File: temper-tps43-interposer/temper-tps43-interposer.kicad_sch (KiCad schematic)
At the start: 5 parts, among them CON1 TPS43 FFC 6-pin

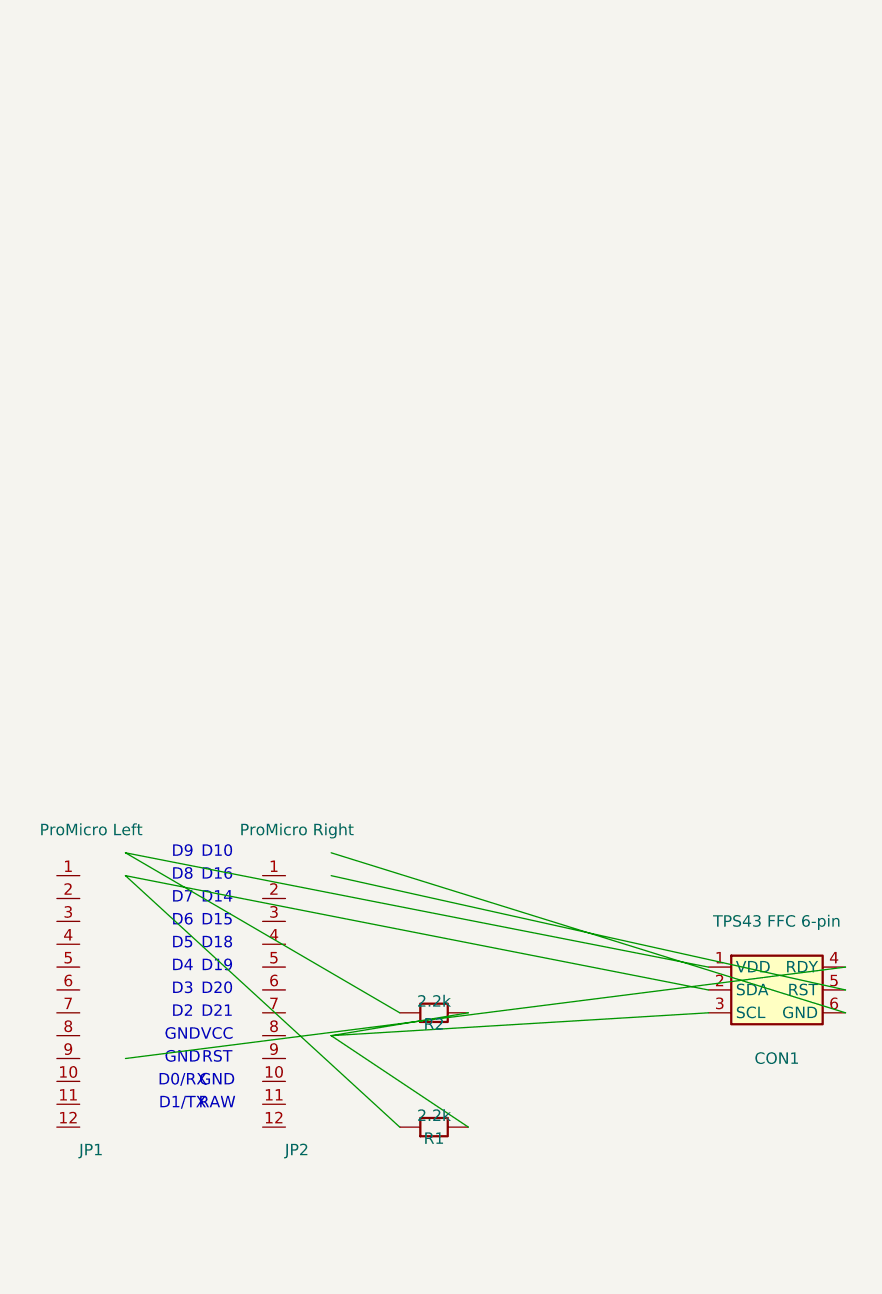
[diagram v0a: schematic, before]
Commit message: Rewrite schematic from scratch: clean KiCAD 9 format, standard symbols only
- JP1, JP2: Connector_Generic:Conn_01x12
- CON1: Connector_Generic:Conn_01x06
- R1, R2: Device:R_Small
- No custom symbol library references
- All symbols defined inline in lib_symbols section
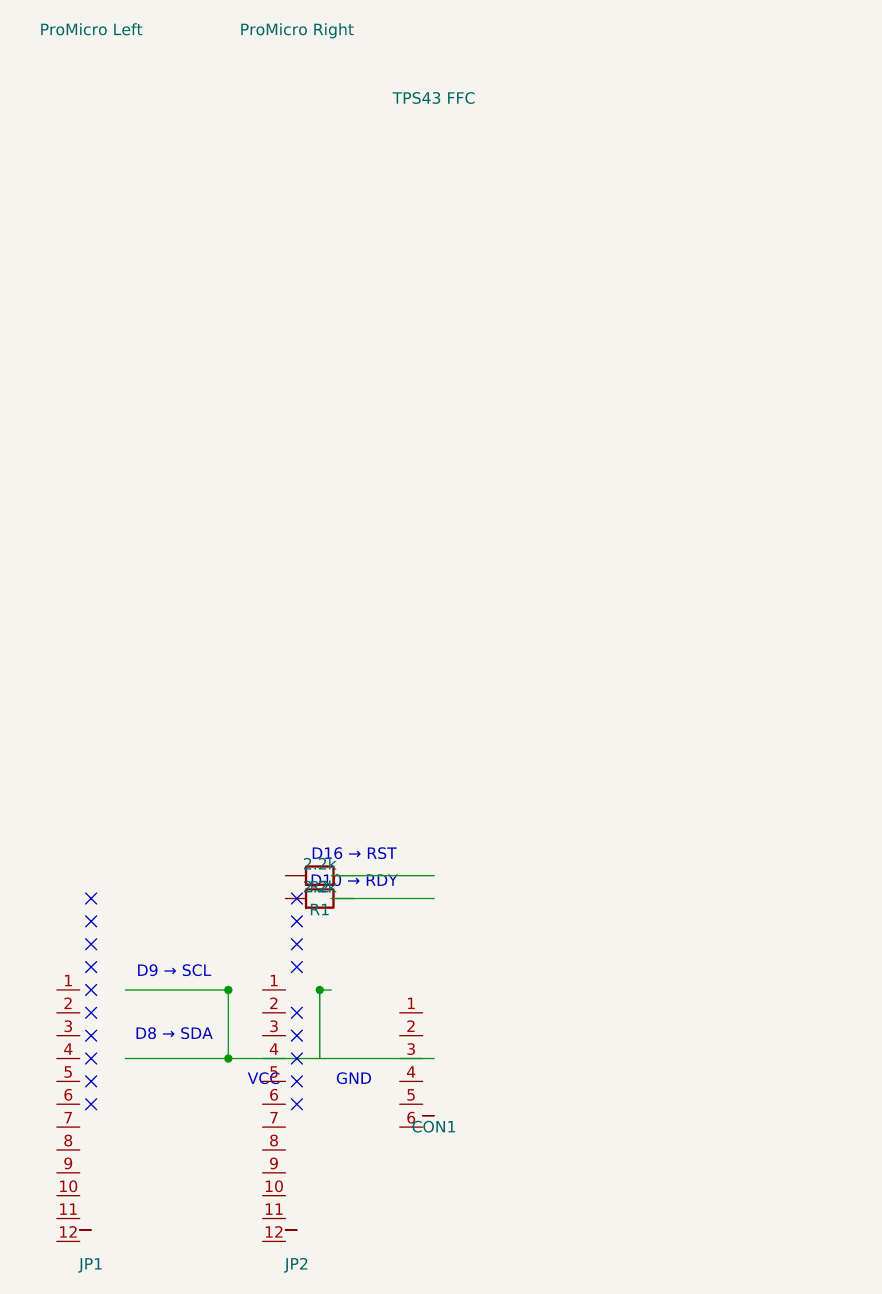
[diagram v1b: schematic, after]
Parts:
- removed CON1: TPS43 FFC 6-pin, symbol temper-tps43-interposer:TPS43_FFC_06
- added CON1: TPS43 FFC, temper-tps43-interposer:TPS43_FFC_06, symbol Connector_Generic:Conn_01x06
- JP1, JP2: footprint (none) -> Connector_PinHeader_2.54mm:PinHeader_1x12_P2.54mm_Vertical
- R1, R2: footprint (none) -> Resistor_SMD:R_0805_2012Metric
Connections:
- net at R1.2: no longer R2.2
- no-connect marks 0 -> 19
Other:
- note added: "D10 → RDY"
- note added: "D16 → RST"
- note added: "D8 → SDA"
- note added: "D9 → SCL"
- note removed: "D0/RX"
- note removed: "D1/TX"
- note removed: "D10"
- note removed: "D14"
- note removed: "D15"
- note removed: "D16"
- note removed: "D18"
- note removed: "D19"
- note removed: "D2"
- note removed: "D20"
- note removed: "D21"
- note removed: "D3"
- note removed: "D4"
- note removed: "D5"
- note removed: "D6"
- note removed: "D7"
- note removed: "D8"
- note removed: "D9"
- note removed: "RAW"
- note removed: "RST"

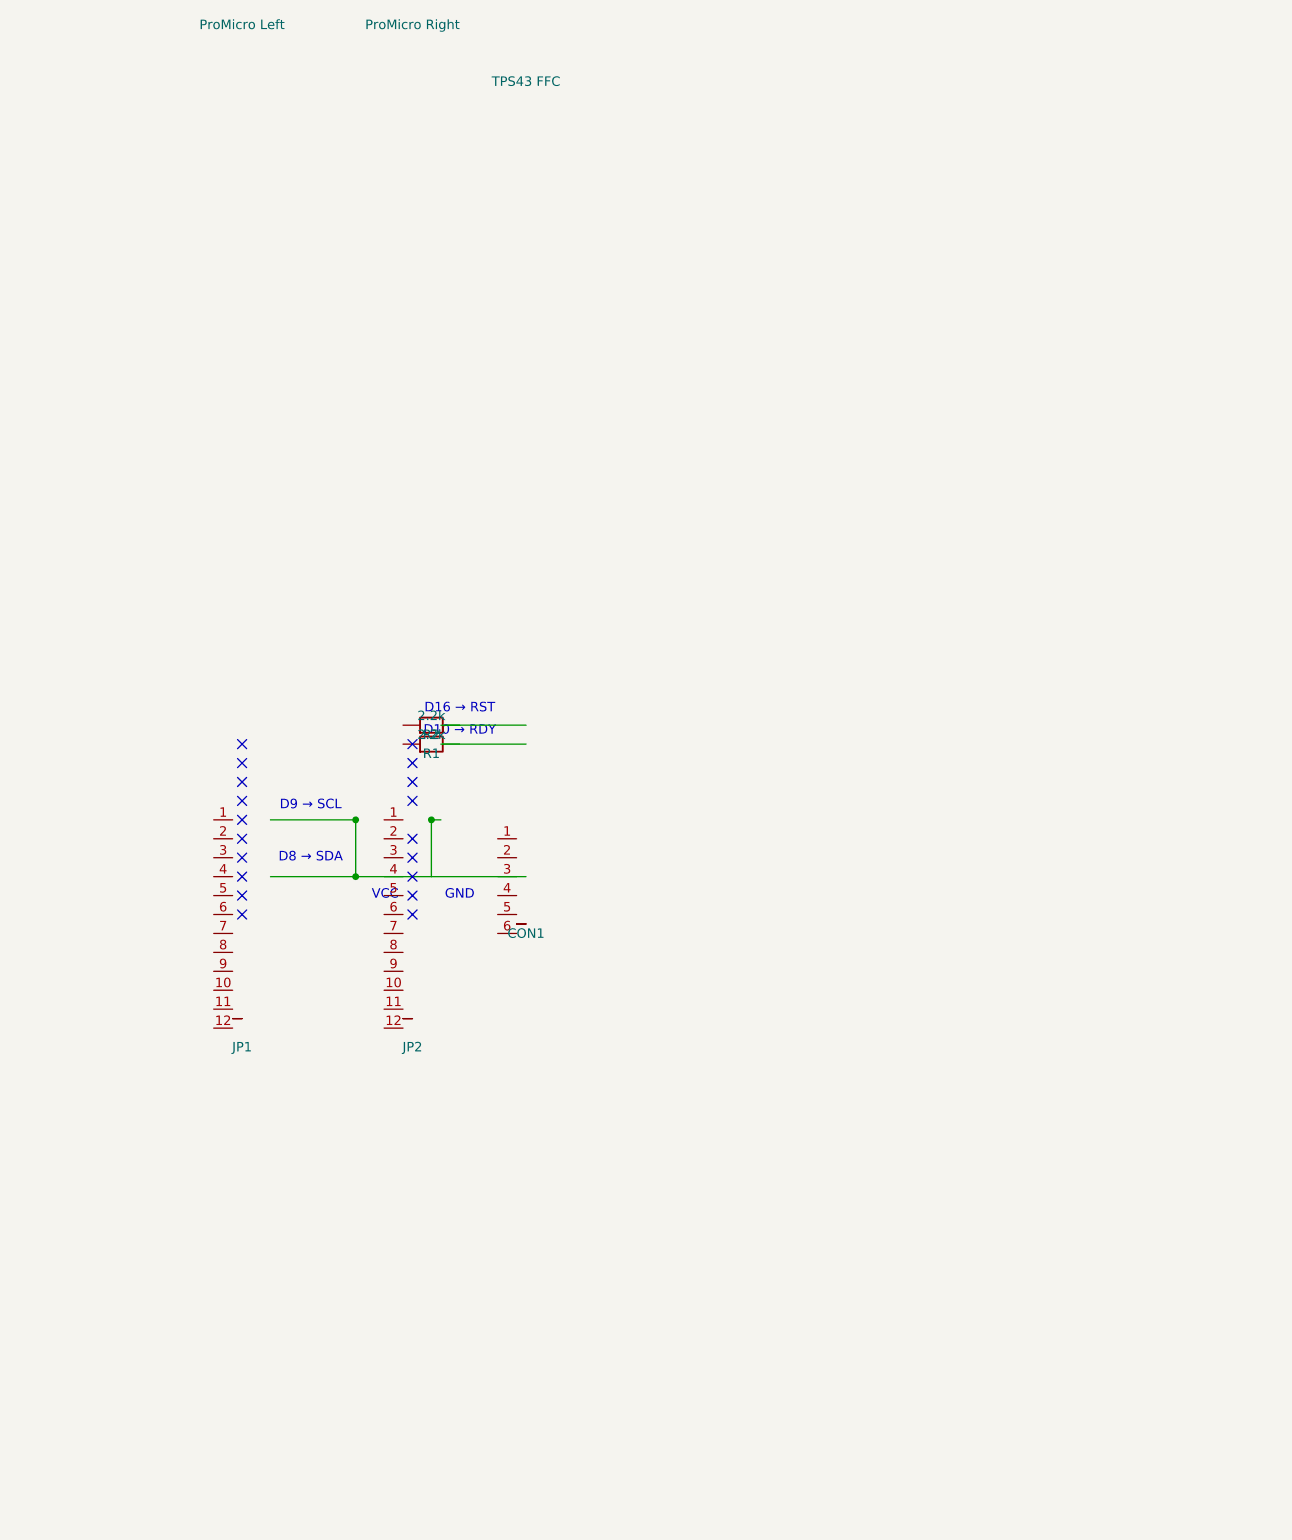
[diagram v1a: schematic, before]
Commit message: Rebuild TPS43 interposer from scratch for KiCad 10
Replaces the hand-written KiCad 9 board with a generated one. gen_schematic.py
owns the netlist table and gen_interposer.py imports it, so the schematic and
the board cannot drift. build.sh gates on ERC, DRC and schematic parity, all of
which are clean.

Sized and verified against the actual Temper hardware (raeedcho/temper) rather
than the old spec:

- 20.0 x 40.0 mm, down from 34 x 44. Temper's choc hotswap sockets end 1.60 mm
  from the controller footprint, so the old width sat 6.44 mm over the adjacent
  switch column and overhung the right board edge by 6.76 mm.
- Notched south edge to clear Temper's nice!view header J2, which starts level
  with header pin 12.
- D8/D9/D10/D16 confirmed unconnected in Temper's netlist.

Corrected errors carried over from the old spec:

- FFC pinout was invented. The TPS43's J1 is 1:RDY 2:NRST 3:GND 4:VDDHI 5:SCL
  6:SDA (datasheet rev 1.06). The old order matched neither that nor its
  reversal, and would have driven 3.3 V onto RDY and shorted SCL to ground.
  CON1 is now derived from TPS43_J1 and checked by verify_pinout().
- D9 is P1.06, D10 is P0.09, D16 is P0.10. The overlay's TWIM_SCL psel was on
  P0.09, which is D10, so I2C could never have come up. P0.11, claimed for D10,
  is D7, one of Temper's matrix rows.
- CONFIG_NFCT_PINS_AS_GPIOS is required: RDY and NRST land on the NFC pins.
- Temper uses Mill-Max 310 machine sockets, which 2.54 mm square header pins do
  not fit. BOM is now Mill-Max pins and sockets.
- R1/R2 at 2.5 mm spacing collided; 0805 courtyard is 3.36 x 1.9 mm.
- Custom Molex footprint used non-plated mounting holes, giving the connector no
  retention. Replaced with the stock Hirose FH12-6S-0.5SH footprint.
- Headers on the wrong faces. Sockets go on top, pins on the bottom.

Open item: the FFC cable mapping cannot be resolved from any datasheet. The
board assumes a reversed cable (CON1 pin N to TPS43 pin 7-N) and the docs
describe the continuity chec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
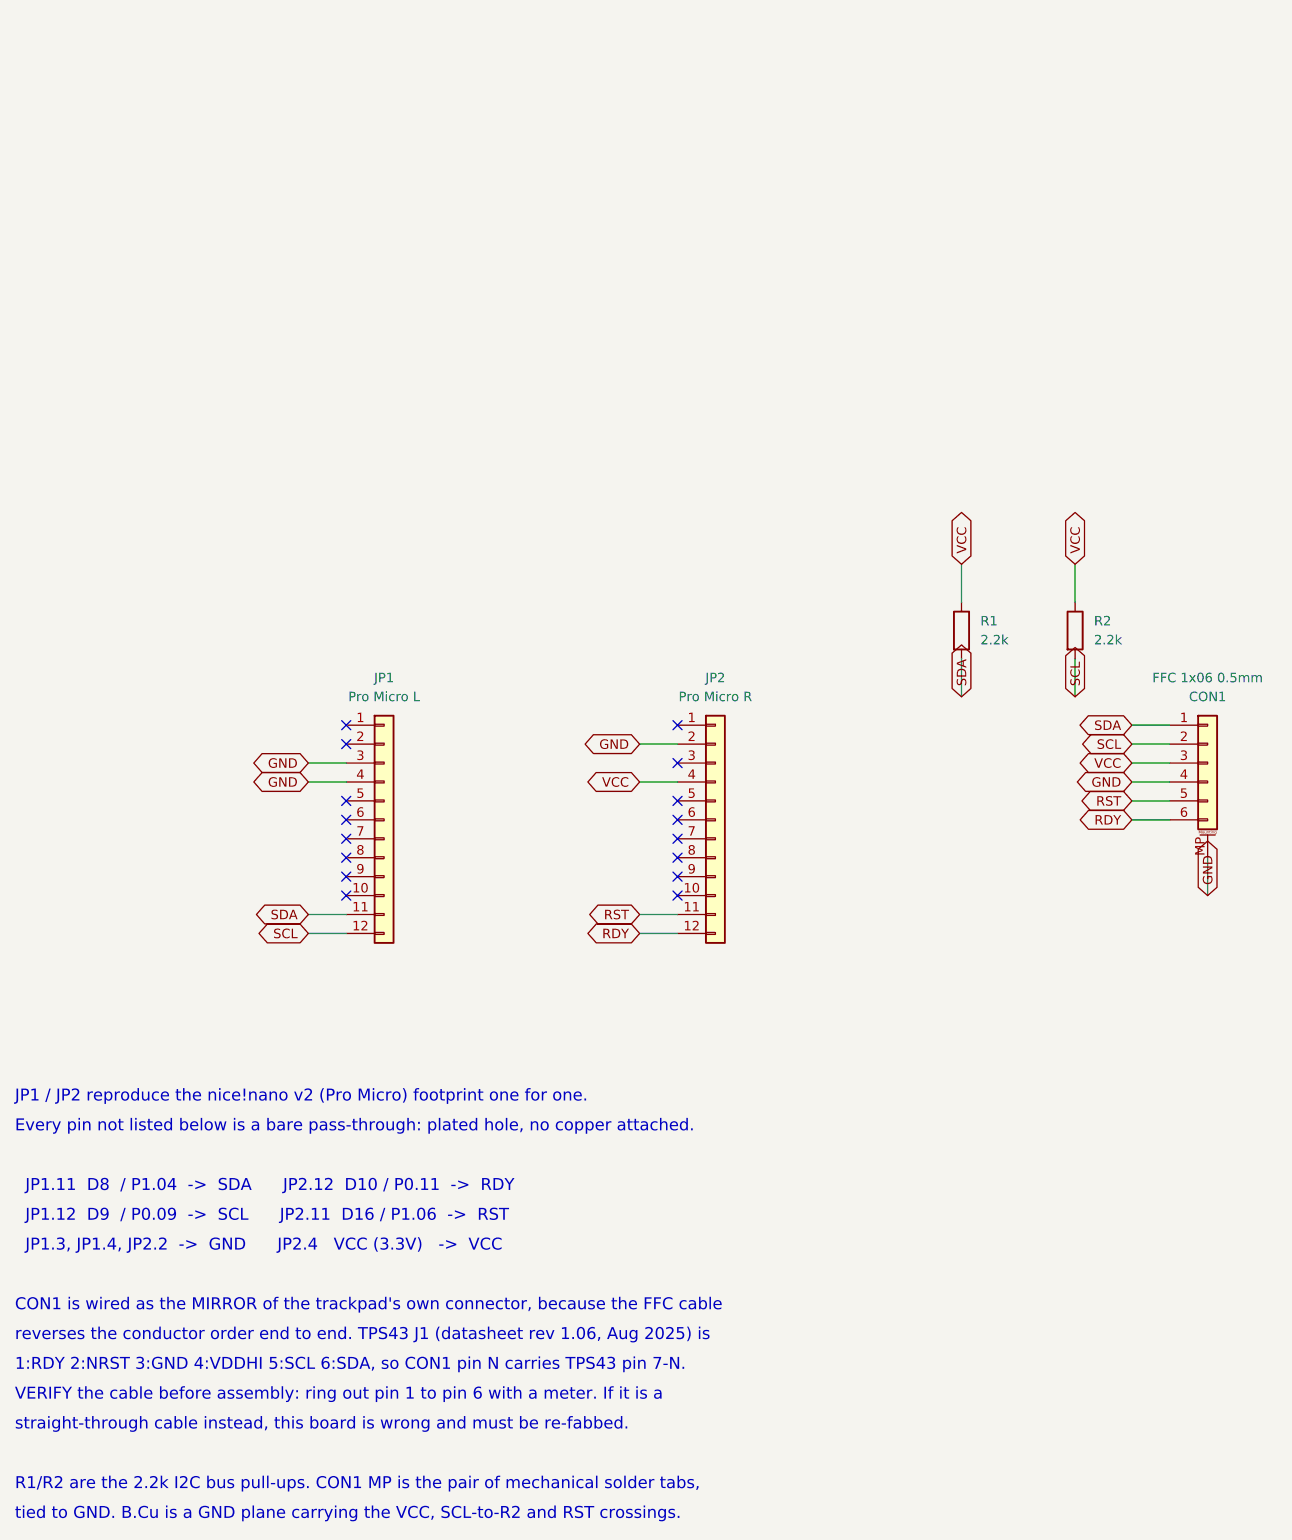
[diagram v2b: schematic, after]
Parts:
- removed CON1: TPS43 FFC, temper-tps43-interposer:TPS43_FFC_06, symbol Connector_Generic:Conn_01x06
- removed R1, R2: 2.2k, Resistor_SMD:R_0805_2012Metric, symbol Device:R_Small
- added CON1: FFC 1x06 0.5mm, Connector_FFC-FPC:Hirose_FH12-6S-0.5SH_1x06-1MP_P0.50mm_Horizontal, symbol Connector_Generic_MountingPin:Conn_01x06_MountingPin
- added R1, R2: 2.2k, Resistor_SMD:R_0805_2012Metric, symbol Device:R
- JP1: value ProMicro Left -> Pro Micro L
- JP2: value ProMicro Right -> Pro Micro R
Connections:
- net SDA: now reaches JP1.11 (Pin_11)
- net SDA: now also CON1.1 (Pin_1), R1.2
- net SCL: now reaches JP1.12 (Pin_12)
- net SCL: now also CON1.2 (Pin_2), R2.2
- net GND: now reaches JP1.3 (Pin_3)
- net GND: now also JP1.4 (Pin_4), JP2.2 (Pin_2), CON1.4 (Pin_4), CON1.MP (MountPin)
- net RST: now reaches JP2.11 (Pin_11)
- net RST: now also CON1.5 (Pin_5)
- net RDY: now reaches JP2.12 (Pin_12)
- net RDY: now also CON1.6 (Pin_6)
- net VCC: now reaches JP2.4 (Pin_4)
- net VCC: now also CON1.3 (Pin_3), R1.1, R2.1
- no-connect marks 19 -> 16
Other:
- note added: "1:RDY 2:NRST 3:GND 4:VDDHI 5:SCL 6:SDA, so CON1 pin N carries TPS43 pin 7-N."
- note added: "CON1 is wired as the MIRROR of the trackpad's own connector, because the FFC cable"
- note added: "Every pin not listed below is a bare pass-through: plated hole, no copper attached."
- note added: "JP1 / JP2 reproduce the nice!nano v2 (Pro Micro) footprint one for one."
- note added: "JP1.11 D8 / P1.04 -> SDA JP2.12 D10 / P0.11 -> RDY"
- note added: "JP1.12 D9 / P0.09 -> SCL JP2.11 D16 / P1.06 -> RST"
- note added: "JP1.3, JP1.4, JP2.2 -> GND JP2.4 VCC (3.3V) -> VCC"
- note added: "R1/R2 are the 2.2k I2C bus pull-ups. CON1 MP is the pair of mechanical solder tabs,"
- note added: "VERIFY the cable before assembly: ring out pin 1 to pin 6 with a meter. If it is a"
- note added: "reverses the conductor order end to end. TPS43 J1 (datasheet rev 1.06, Aug 2025) is"
- note added: "straight-through cable instead, this board is wrong and must be re-fabbed."
- note added: "tied to GND. B.Cu is a GND plane carrying the VCC, SCL-to-R2 and RST crossings."
- note removed: "D10 → RDY"
- note removed: "D16 → RST"
- note removed: "D8 → SDA"
- note removed: "D9 → SCL"
- note removed: "GND"
- note removed: "VCC"
